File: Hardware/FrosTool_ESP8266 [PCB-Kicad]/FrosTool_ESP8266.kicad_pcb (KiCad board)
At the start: 2 copper layers, 25.4 x 25.4 mm, 37 parts, among them J1 IN_PANEL, J10 V3.3, J11 V3.3, J12 V3.3, J13 GND, J14 GND, J15 GND, J2 BATERIA, J3 TX_RX, J4 GPIO13(D)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

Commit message: components located
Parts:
- C1, C2, C3, C4, Q1, R1, R2, R3, R4, R5, R6, R7, R8, R9, U1, U3: moved to B.Cu
- moved J13 57.5 mm to (69.6, 49.8)
- moved J14 52.4 mm to (72.4, 49.8)
- moved R5 50.0 mm to (65.9, 29.8)
- moved R9 49.1 mm to (65.8, 26.8)
- moved C2 49.1 mm to (54.1, 42.2)
- moved J1 48.2 mm to (68.5, 46.2), turned to 270 degrees
- moved J15 47.9 mm to (75.2, 49.8)
- moved J5 46.9 mm to (75.2, 44.7)
- moved J4 45.7 mm to (66.8, 49.8)
- moved J7 44.8 mm to (63.5, 49.8)
- moved J3 44.5 mm to (74.9, 26.4)
- moved R7 41.9 mm to (70.8, 29.8)
- moved J9 41.2 mm to (75.2, 47.2)
- moved R1 41.0 mm to (55.7, 26.8)
- moved U1 40.6 mm to (70.1, 40.7)
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
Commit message: AutoRuting
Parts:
- added Drill222_2: SolderWirePad_single_1-2mmDrill, Wire_Pads:SolderWirePad_single_1-2mmDrill, F.Cu at (74.9, 26.7)
- added Drill2mm_1: SolderWirePad_single_1-2mmDrill, Wire_Pads:SolderWirePad_single_1-2mmDrill, F.Cu at (52.1, 26.7)
- moved J3 2.95 mm to (74.9, 29.4)
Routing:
- net GND: track 0.00 -> 111.9 mm, vias 0 -> 2
- net +3V3: track 0.00 -> 76.4 mm, vias 0 -> 1
- net BAT+: track 0.00 -> 48.7 mm
- net Net-(C3-Pad2): track 0.00 -> 33.4 mm, vias 0 -> 1
- net Net-(D3-Pad1): track 0.00 -> 32.4 mm, vias 0 -> 1
- net Net-(R1-Pad1): track 0.00 -> 31.9 mm, vias 0 -> 2
- net /GPIO13: track 0.00 -> 27.0 mm
- net /GPIO4: track 0.00 -> 27.0 mm, vias 0 -> 1
- net Net-(D1-Pad2): track 0.00 -> 24.7 mm, vias 0 -> 1
- net Net-(R3-Pad2): track 0.00 -> 24.0 mm, vias 0 -> 2
- net /GPIO12: track 0.00 -> 21.4 mm
- net IN+: track 0.00 -> 19.8 mm, vias 0 -> 1
- net Net-(R9-Pad1): track 0.00 -> 19.3 mm
- net /GPIO5: track 0.00 -> 18.5 mm
- net Net-(D2-Pad1): track 0.00 -> 17.5 mm
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
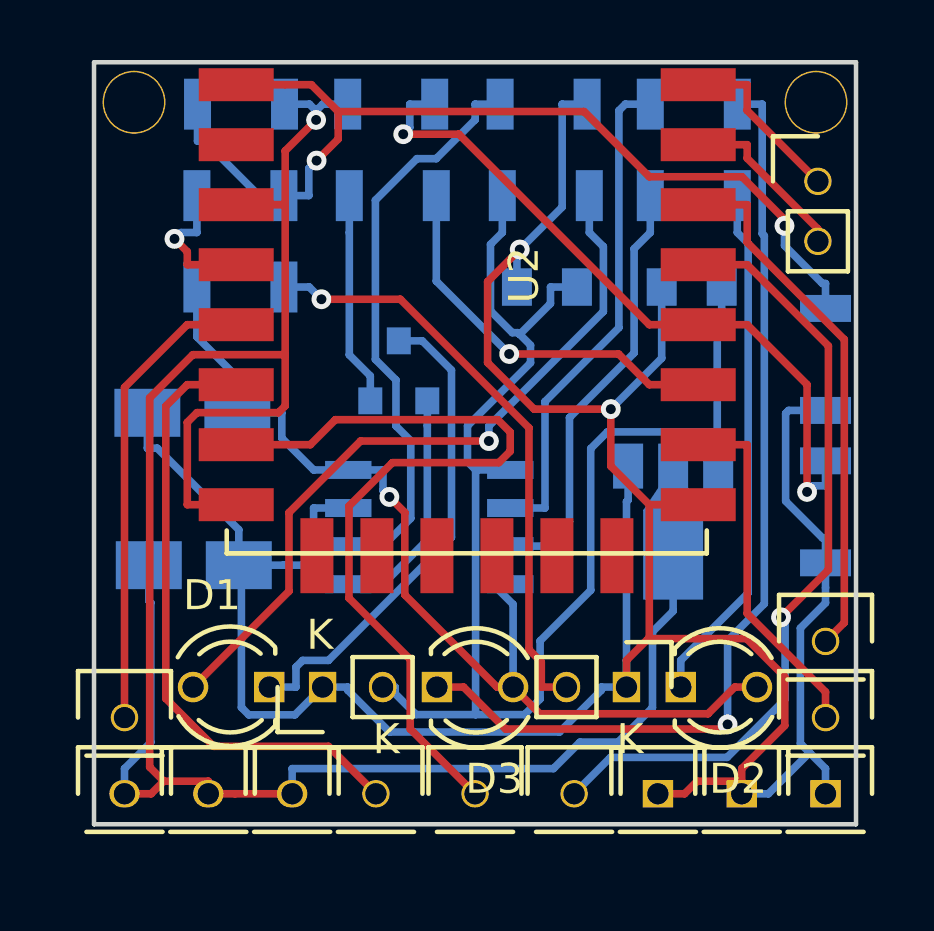
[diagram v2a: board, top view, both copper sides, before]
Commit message: Tracks and Vias improvement Bug Fixed: Pads Regulator
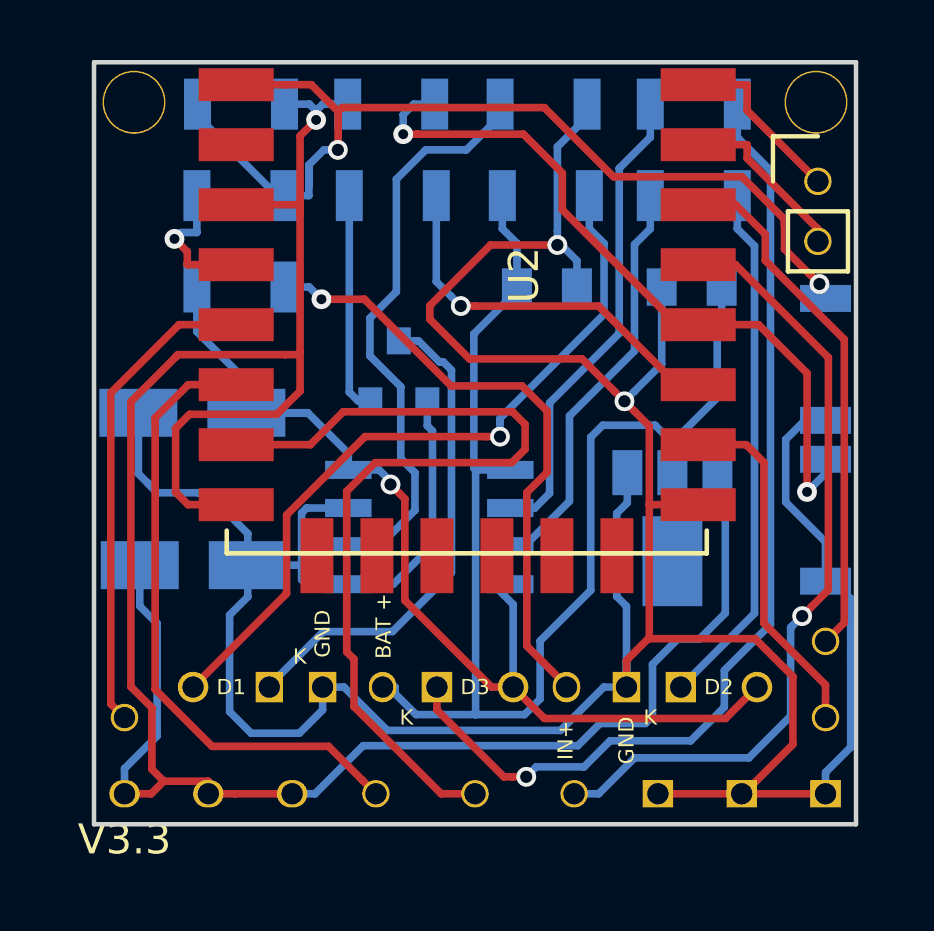
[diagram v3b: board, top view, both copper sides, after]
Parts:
- C2, C3: footprint Capacitors_SMD:c_elec_3x5.3 -> Capacitors_SMD:c_elec_4x5.3
- U1: value AP1117-33 -> HT7333-1
- moved SW2 0.28 mm to (75.2, 40.7)
- moved U1 0.22 mm to (70.1, 40.9)
- turned C4 to 180 degrees
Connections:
- U1 pad 2: +3V3 -> BAT+
- U1 pad 3: BAT+ -> +3V3
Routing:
- net GND: track 111.9 -> 119.6 mm
- net +3V3: track 76.4 -> 80.6 mm
- net BAT+: track 48.7 -> 44.7 mm
- net /GPIO13: track 27.0 -> 29.4 mm
- net Net-(C3-Pad2): track 33.4 -> 35.6 mm
- net Net-(R3-Pad2): track 24.0 -> 25.7 mm
- net Net-(D3-Pad1): track 32.4 -> 33.4 mm
- net IN+: track 19.8 -> 20.5 mm
- net Net-(R1-Pad1): track 31.9 -> 32.7 mm
- net Net-(R8-Pad1): track 16.6 -> 15.9 mm
- net /GPIO14: track 16.3 -> 16.8 mm

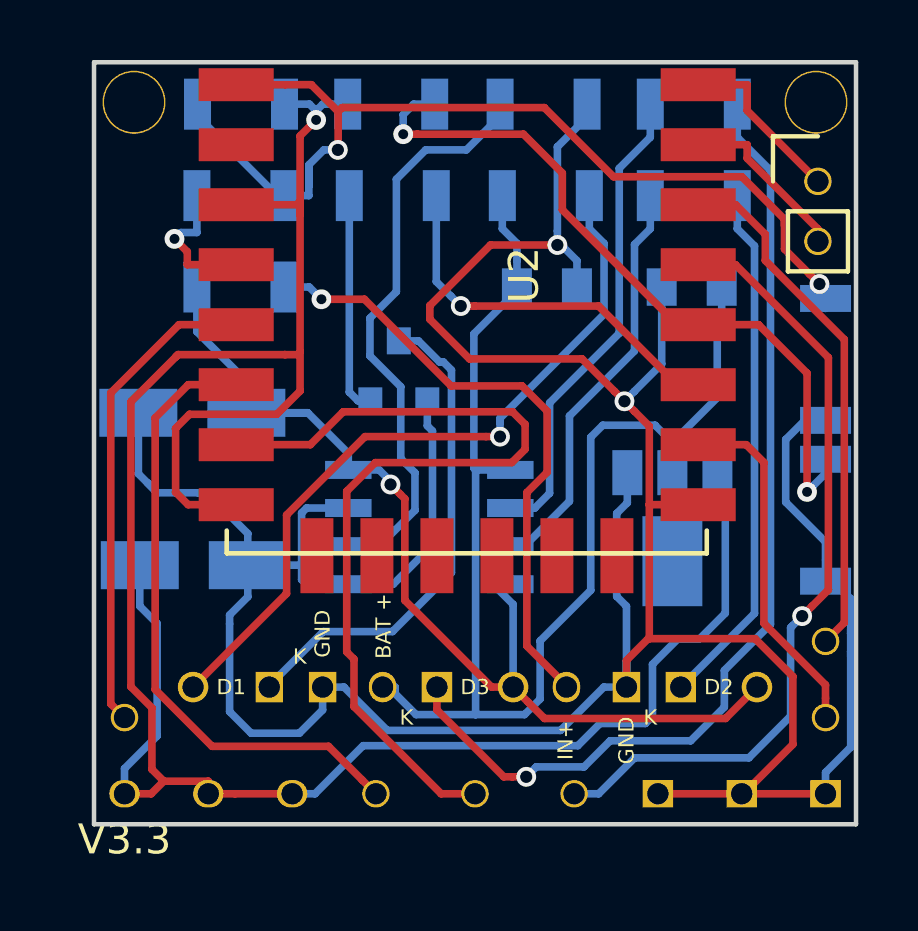
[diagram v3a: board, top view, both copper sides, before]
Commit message: Added zones (F.cu, B.cu -> GND)
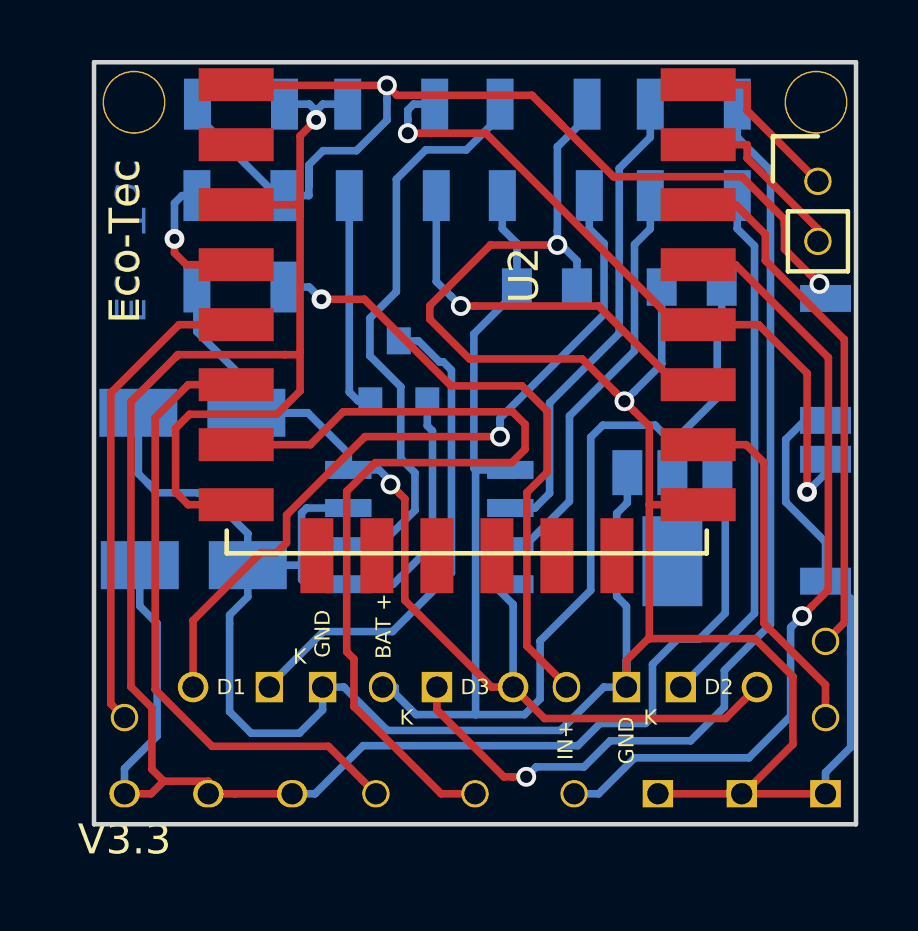
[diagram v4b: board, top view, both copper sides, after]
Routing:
- net Net-(R1-Pad1): track 32.7 -> 36.2 mm
- net Net-(R3-Pad2): track 25.7 -> 24.7 mm
- added copper zone on B.Cu, net GND
- added copper zone on F.Cu, net GND
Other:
- board text added: "Eco-Tec"

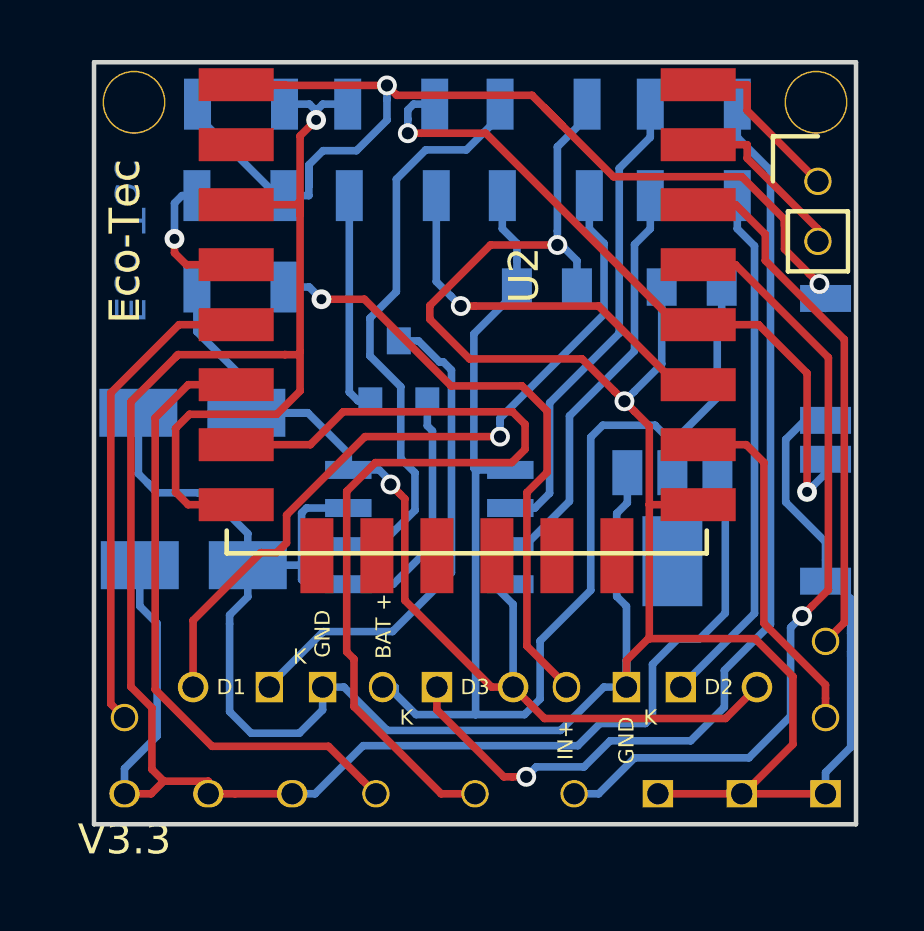
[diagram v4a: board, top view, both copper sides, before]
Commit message: F.Fab, B.Fab
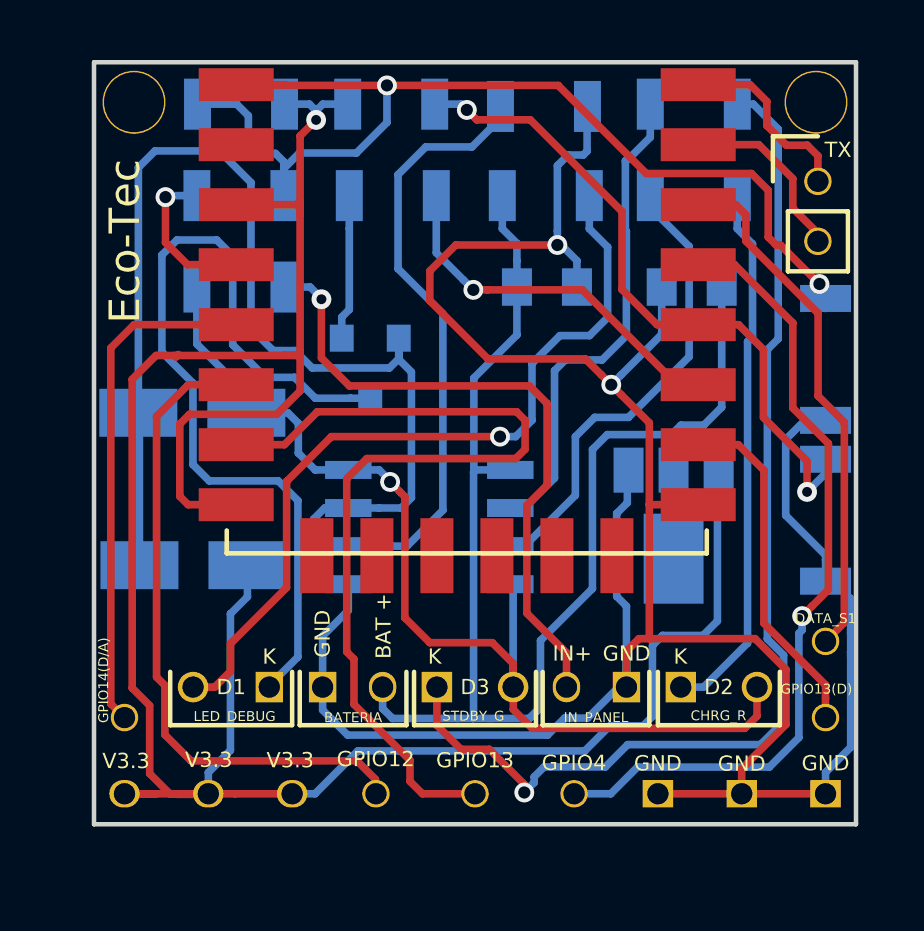
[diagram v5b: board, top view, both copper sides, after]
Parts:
- moved Q1 0.96 mm to (60.0, 35.6), turned to 270 degrees
- moved U1 0.09 mm to (70.1, 40.8)
- moved R9 0.08 mm to (65.8, 26.9)
- turned C2 to 180 degrees
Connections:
- Q1 pad 1: GND -> Net-(Q1-Pad1)
- Q1 pad 2: Net-(Q1-Pad2) -> GND
- R4 pad 1: Net-(Q1-Pad2) -> Net-(Q1-Pad1)
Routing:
- net Net-(D1-Pad1): track 16.6 -> 29.1 mm
- net GND: track 119.6 -> 131.7 mm
- net Net-(Q1-Pad2): track 7.37 -> 0.00 mm
- net Net-(Q1-Pad1): track 0.00 -> 4.86 mm
- net +3V3: track 80.6 -> 84.3 mm
- net Net-(D3-Pad1): track 33.4 -> 36.8 mm
- net Net-(D1-Pad2): track 25.2 -> 27.0 mm
- net Net-(R7-Pad1): track 13.9 -> 15.6 mm
- net IN+: track 20.5 -> 21.8 mm
- net Net-(R3-Pad2): track 24.7 -> 23.6 mm
- net BAT+: track 44.7 -> 45.8 mm
- net /GPIO12: track 21.7 -> 22.6 mm
- net /GPIO14: track 16.8 -> 17.7 mm
- net /GPIO13: track 29.4 -> 30.1 mm
- net Net-(R9-Pad1): track 19.5 -> 20.1 mm
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
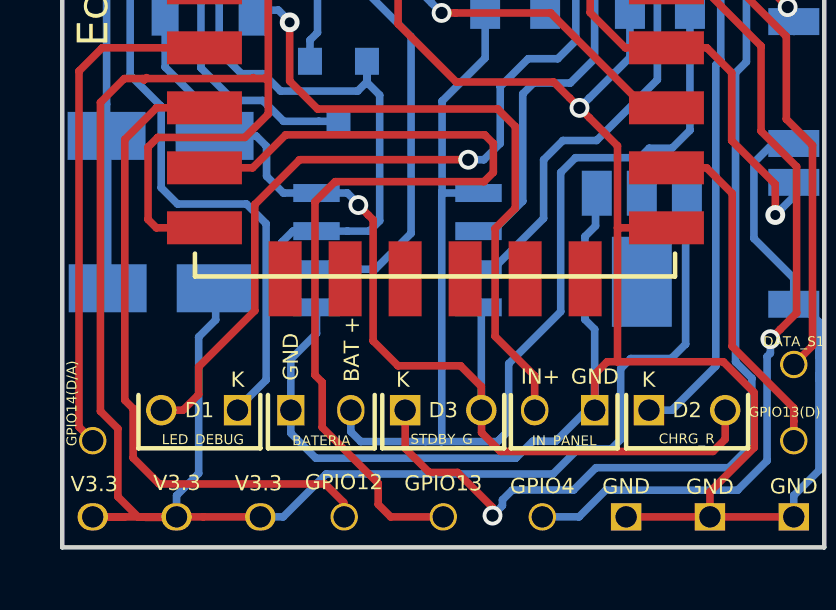
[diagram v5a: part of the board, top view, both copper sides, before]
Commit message: Added Pin Extra: BAT+
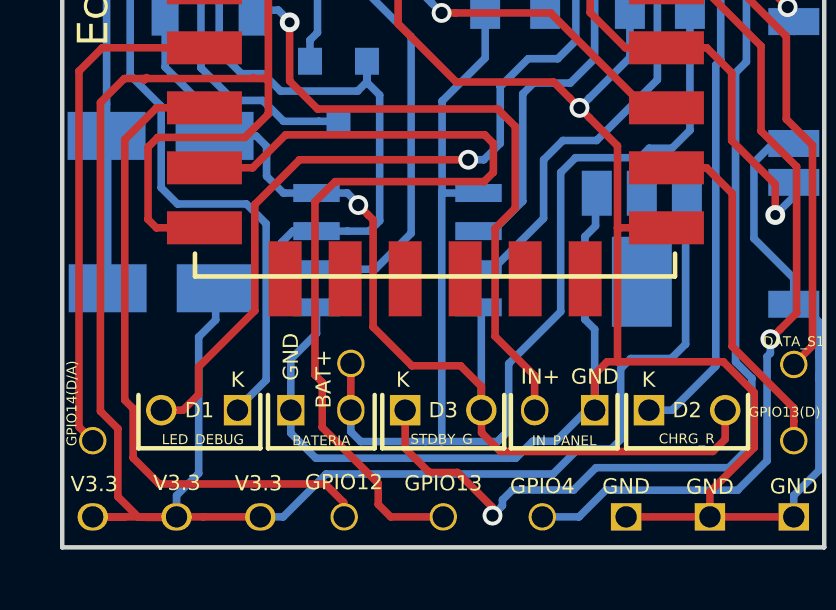
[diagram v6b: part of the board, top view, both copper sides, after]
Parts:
- added J16: BAT+, Pin_Headers:Pin_Header_Straight_1x01, F.Cu at (60.4, 44.7)
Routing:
- net BAT+: track 45.8 -> 47.3 mm
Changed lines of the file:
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@@
 (kicad_pcb (version 4) (host pcbnew 4.0.5+dfsg1-4)
   (general
-    (links 58)
+    (links 59)
     (no_connects 0)
     (area 37.114175 17.068199 86.075825 50.875001)
     (thickness 1.6)
     (drawings 6)
-    (tracks 461)
+    (tracks 463)
     (zones 0)
-    (modules 39)
+    (modules 40)
     (nets 33)
   )
@@
     (mod_text_size 1 1)
     (mod_text_width 0.15)
-    (pad_size 1.99898 2.99974)
-    (pad_drill 0)
+    (pad_size 0.9144 0.9144)
+    (pad_drill 0.7112)
     (pad_to_mask_clearance 0.2)
     (aux_axis_origin 0 0)
@@
     (uvia_drill 0.254)
   )
+  (module Pin_Headers:Pin_Header_Straight_1x01 (layer F.Cu)
+    (at 60.42152 44.66844)
+    (descr "Through hole pin header")
+    (tags "pin header")
+    (fp_text reference J16 (at 0 1.27) (layer F.Fab) hide
+      (effects (font (size 0.508 0.508) (thickness 0.127)))
+    )
+    (fp_text value BAT+ (at -0.90932 0.51816 90) (layer F.SilkS)
+      (effects (font (size 0.508 0.508) (thickness 0.127)))
+    )
+    (pad 1 thru_hole circle (at 0 0) (size 0.9144 0.9144) (drill 0.7112) (layers *.Cu *.Mask)
+      (net 1 BAT+))
+  )
   (module LEDs:LED-3MM placed (layer F.Cu)
     (at 70.358 46.228)
@@
     (fp_line (start -1.27 -0.762) (end -1.27 2.794) (layer F.SilkS) (width 0.15))
     (fp_line (start 0.508 -0.762) (end -1.27 -0.762) (layer F.SilkS) (width 0.15))
-    (fp_text user "BAT +" (at 2.032 2.032 90) (layer F.SilkS)
+    (fp_text user "BAT +" (at 2.032 2.032 90) (layer F.SilkS) hide
       (effects (font (size 0.508 0.508) (thickness 0.127)))
     )
@@
   (gr_line (start 76.2 25.4) (end 76.2 50.8) (layer Edge.Cuts) (width 0.15))
   (gr_line (start 50.8 25.4) (end 76.2 25.4) (layer Edge.Cuts) (width 0.15))
+  (segment (start 60.42 46.228) (end 60.42 44.66996) (width 0.254) (layer F.Cu) (net 1))
+  (segment (start 60.42 44.66996) (end 60.42152 44.66844) (width 0.254) (layer F.Cu) (net 1))
   (segment (start 70.0786 38.07587) (end 69.81436 37.81163) (width 0.254) (layer B.Cu) (net 1))
   (segment (start 67.909518 37.81163) (end 67.41499 38.306158) (width 0.254) (layer B.Cu) (net 1))
@@
   (segment (start 57.404 49.784) (end 56.9594 49.784) (width 0.254) (layer F.Cu) (net 3))
   (segment (start 58.203 27.3228) (end 58.203 27.0187) (width 0.254) (layer B.Cu) (net 3))
+  (segment (start 64.77 46.228) (end 64.77 45.440747) (width 0.254) (layer F.Cu) (net 4))
+  (segment (start 64.77 45.440747) (end 64.076951 44.747698) (width 0.254) (layer F.Cu) (net 4))
+  (segment (start 60.999374 39.719976) (end 60.669175 39.389777) (width 0.254) (layer F.Cu) (net 4))
+  (segment (start 64.076951 44.747698) (end 62.453632 44.747698) (width 0.254) (layer F.Cu) (net 4))
+  (segment (start 62.453632 44.747698) (end 61.1614 43.455466) (width 0.254) (layer F.Cu) (net 4))
+  (segment (start 61.1614 43.455466) (end 61.1614 39.882002) (width 0.254) (layer F.Cu) (net 4))
+  (segment (start 61.1614 39.882002) (end 60.999374 39.719976) (width 0.254) (layer F.Cu) (net 4))
   (segment (start 55.878 37.084) (end 55.878 36.442811) (width 0.254) (layer B.Cu) (net 4))
   (segment (start 55.878 36.442811) (end 54.229 34.793811) (width 0.254) (layer B.Cu) (net 4))
@@
   (segment (start 65.403735 47.603255) (end 64.776157 46.975677) (width 0.254) (layer F.Cu) (net 4))
   (segment (start 64.776157 46.975677) (end 64.776157 46.234157) (width 0.254) (layer F.Cu) (net 4))
-  (segment (start 64.77 46.228) (end 64.77 45.440747) (width 0.254) (layer F.Cu) (net 4))
-  (segment (start 64.77 45.440747) (end 64.076951 44.747698) (width 0.254) (layer F.Cu) (net 4))
-  (segment (start 64.076951 44.747698) (end 61.991183 44.747698) (width 0.254) (layer F.Cu) (net 4))
-  (segment (start 61.991183 44.747698) (end 61.1614 43.917915) (width 0.254) (layer F.Cu) (net 4))
-  (segment (start 61.1614 43.917915) (end 61.1614 39.882002) (width 0.254) (layer F.Cu) (net 4))
-  (segment (start 61.1614 39.882002) (end 60.999374 39.719976) (width 0.254) (layer F.Cu) (net 4))
-  (segment (start 60.999374 39.719976) (end 60.669175 39.389777) (width 0.254) (layer F.Cu) (net 4))
   (via (at 60.669175 39.389777) (size 0.6604) (drill 0.4064) (layers F.Cu B.Cu) (net 4))
   (segment (start 60.669175 39.353175) (end 60.669175 39.389777) (width 0.254) (layer B.Cu) (net 4))
